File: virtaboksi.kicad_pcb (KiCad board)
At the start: 2 copper layers, 50 x 71.9 mm, 61 parts, among them J1 Panel_01x08, J2 Ext_01x05, J3 Powerpole 01x02, J4 Powerpole 01x02, J5 Powerpole 01x02, J6 Conn_01x03_Male, J7 TagConnect_TC2030-NL, Q1 2N7002, Q2 IRF4905, Q3 IRF4905, Q4 2N7002, Q5 IRF4905, Q6 IRF4905, Q7 2N7002, Q8 IRF4905, Q9 IRF4905, U1 SRV05-4, U2 AMSRI-783.3-NZ, U3 STM8S003F3P, U4 SRV05-4, U5 SP3485EN

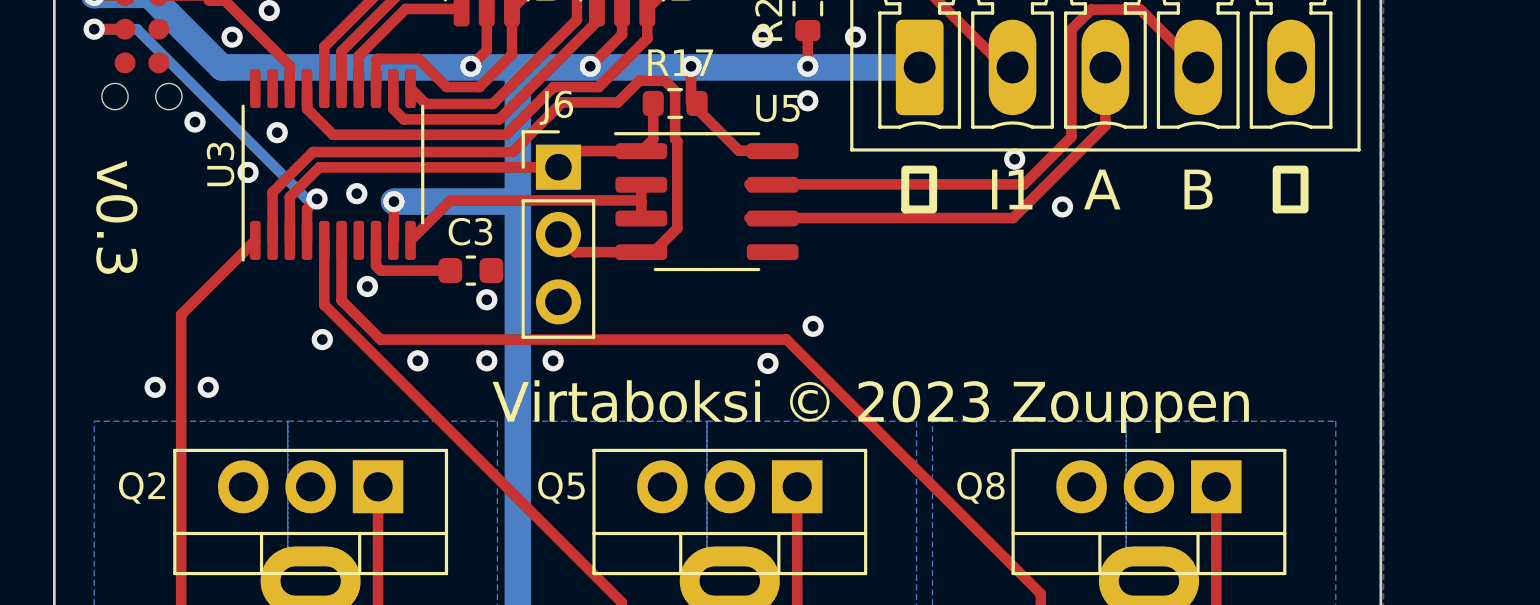
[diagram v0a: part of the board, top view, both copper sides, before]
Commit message: Update silkscreen, change revision to 0.4
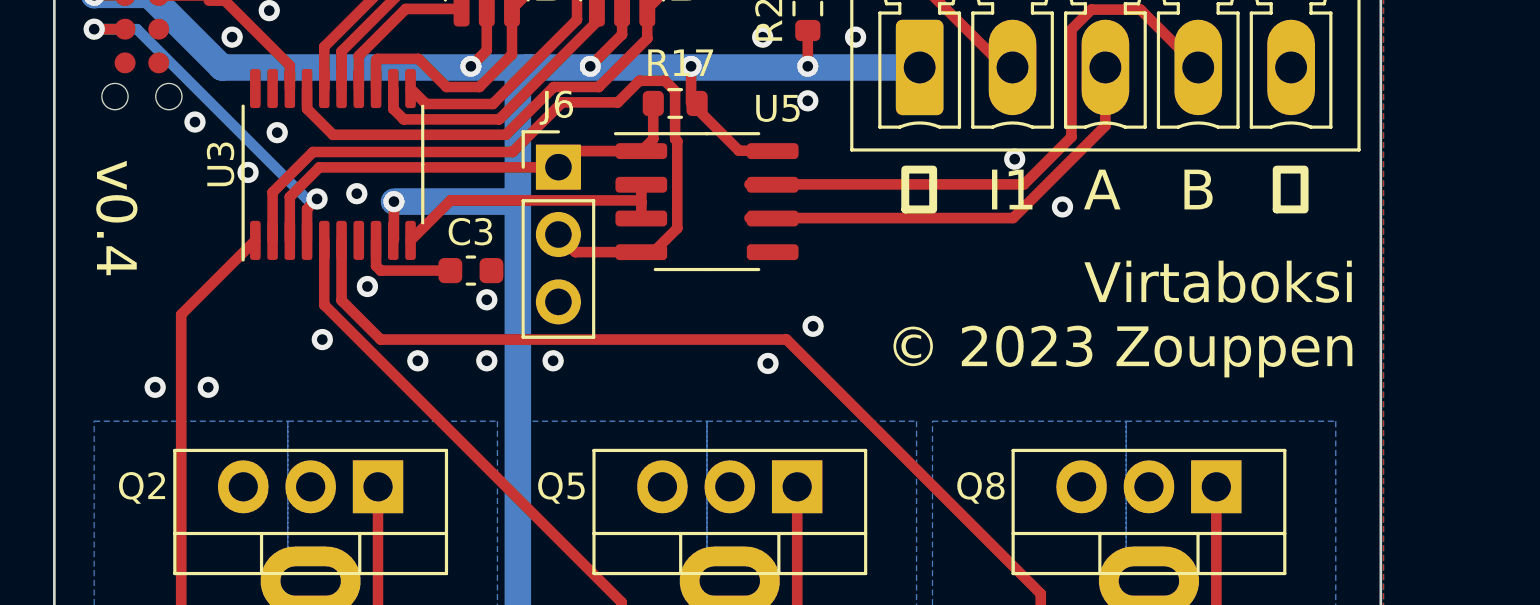
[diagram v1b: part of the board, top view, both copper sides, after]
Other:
- board text added: "${TITLE} © ${COMMENT1} ${COMPANY}"
- board text added: "I2"
- board text added: "I3"
- board text added: "I4"
- board text added: "L1"
- board text added: "L2"
- board text added: "L3"
- board text added: "RX"
- board text added: "TX"
- board text removed: "Virtaboksi © 2023 Zouppen"
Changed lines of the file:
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@@
   (paper "A4")
   (title_block
-    (rev "0.3")
+    (title "Virtaboksi")
+    (date "2023-09-26")
+    (rev "0.4")
+    (company "Zouppen")
+    (comment 1 "2023")
   )
   (layers
@@
     ) (layer "B.Mask") (width 0) (fill solid))
   (gr_rect (start 107.5 40) (end 157.5 111.9) (layer "Edge.Cuts") (width 0.1) (fill none))
+  (gr_text "⏚" (at 128.3 64.7) (layer "B.SilkS")
+    (effects (font (size 1.5 1.5) (thickness 0.3)) (justify right mirror))
+  )
+  (gr_text "I4" (at 125.6 48.6) (layer "B.SilkS")
+    (effects (font (size 1.5 1.5) (thickness 0.3)) (justify mirror))
+  )
+  (gr_text "I3" (at 122.2 48.6) (layer "B.SilkS")
+    (effects (font (size 1.5 1.5) (thickness 0.3)) (justify mirror))
+  )
+  (gr_text "L3" (at 139.7 48.7) (layer "B.SilkS")
+    (effects (font (size 1.5 1.5) (thickness 0.3)) (justify mirror))
+  )
+  (gr_text "⏚" (at 129.2 48.6) (layer "B.SilkS")
+    (effects (font (size 1.5 1.5) (thickness 0.3)) (justify mirror))
+  )
+  (gr_text "TX" (at 128.2 61.9) (layer "B.SilkS")
+    (effects (font (size 1.5 1.5) (thickness 0.3)) (justify right mirror))
+  )
+  (gr_text "⏚" (at 143.2 48.6) (layer "B.SilkS")
+    (effects (font (size 1.5 1.5) (thickness 0.3)) (justify mirror))
+  )
+  (gr_text "RX" (at 128.3 59.5) (layer "B.SilkS")
+    (effects (font (size 1.5 1.5) (thickness 0.3)) (justify right mirror))
+  )
+  (gr_text "L2" (at 136.1 48.6) (layer "B.SilkS")
+    (effects (font (size 1.5 1.5) (thickness 0.3)) (justify mirror))
+  )
+  (gr_text "L1" (at 132.6 48.6) (layer "B.SilkS")
+    (effects (font (size 1.5 1.5) (thickness 0.3)) (justify mirror))
+  )
+  (gr_text "I2" (at 118.7 48.6) (layer "B.SilkS")
+    (effects (font (size 1.5 1.5) (thickness 0.3)) (justify mirror))
+  )
   (gr_text "⏚" (at 154.1 60.3) (layer "F.SilkS")
     (effects (font (size 1.5 1.5) (thickness 0.3)))
@@
     (effects (font (size 1.5 1.5) (thickness 0.3)))
   )
-  (gr_text "Virtaboksi © 2023 Zouppen" (at 124 68.3) (layer "F.SilkS")
-    (effects (font (size 1.5 1.5) (thickness 0.3)) (justify left))
+  (gr_text "${TITLE}\n© ${COMMENT1} ${COMPANY}" (at 156.6 65) (layer "F.SilkS")
+    (effects (font (size 1.5 1.5) (thickness 0.3)) (justify right))
   )
   (gr_text "I1" (at 143.6 60.3) (layer "F.SilkS")

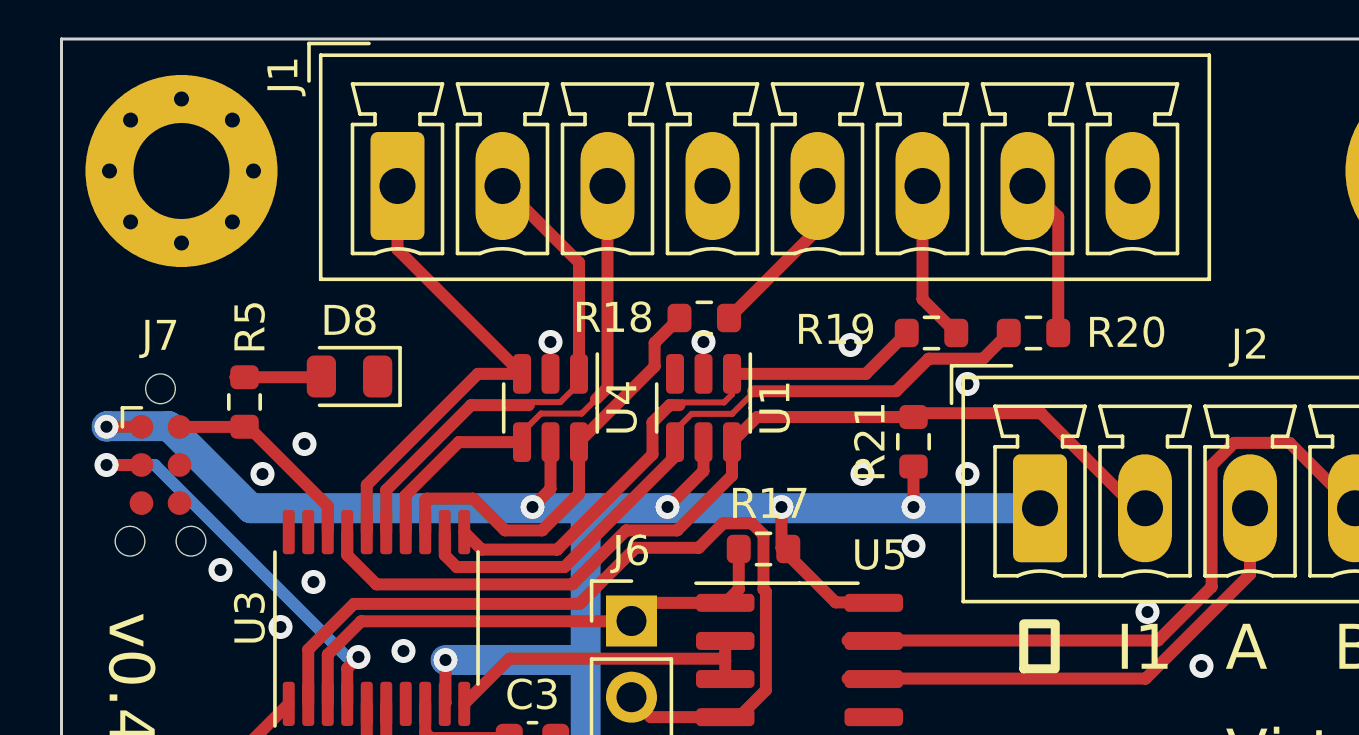
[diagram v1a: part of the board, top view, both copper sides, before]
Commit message: Minor cosmetic PCB changes
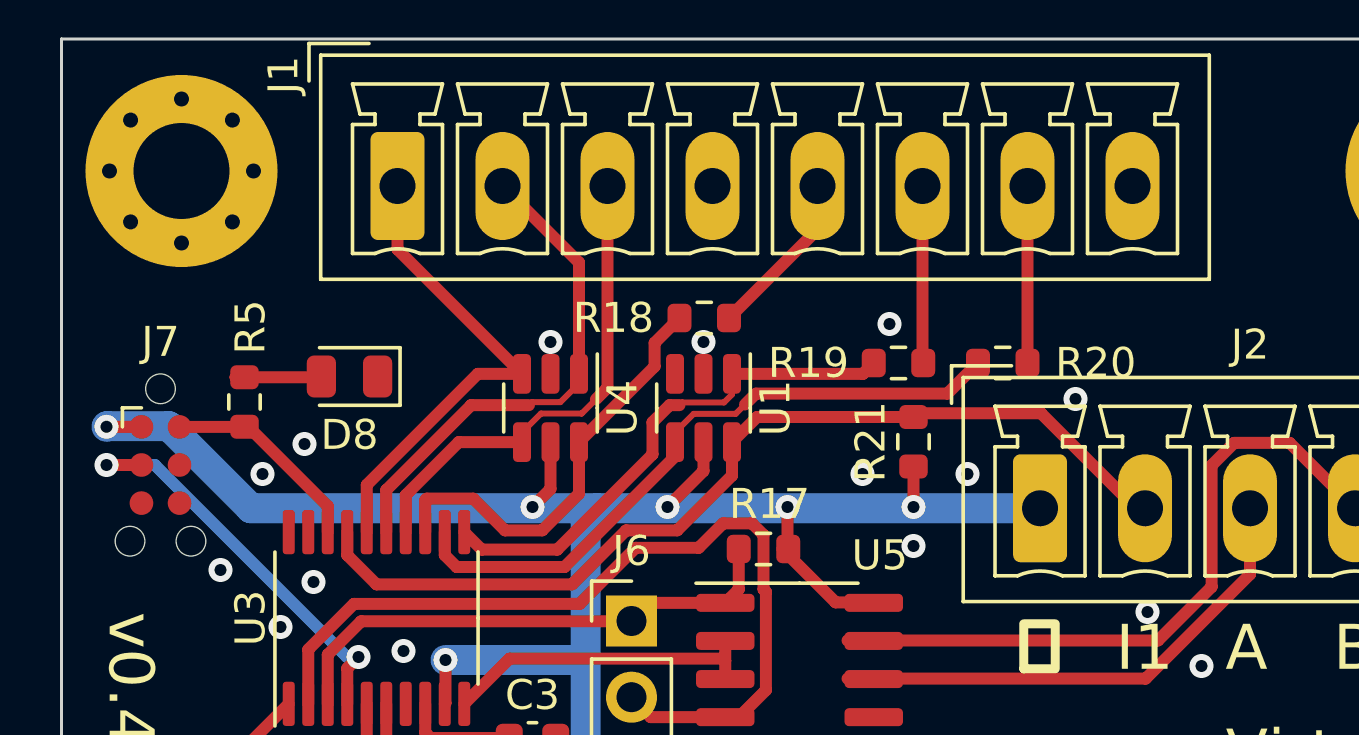
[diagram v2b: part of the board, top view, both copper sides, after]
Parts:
- moved R19 1.49 mm to (135.4, 50.8)
- moved R20 1.43 mm to (138.9, 50.8)
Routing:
- net /LED2: track 19.0 -> 17.5 mm
- net /LED3: track 23.5 -> 22.4 mm
- net Net-(J1-Pad7): track 5.32 -> 5.90 mm
- net Net-(J1-Pad6): track 5.37 -> 5.91 mm
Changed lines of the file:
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@@
     (property "Sheetname" "")
     (attr exclude_from_pos_files)
-    (fp_text reference "J7" (at -4.3 0 180) (layer "F.SilkS")
+    (fp_text reference "J7" (at -4.1 0 180) (layer "F.SilkS")
       (effects (font (size 1 1) (thickness 0.15)))
     )
@@
     (property "Sheetname" "")
     (attr smd)
-    (fp_text reference "D8" (at 0 1.85) (layer "F.SilkS")
+    (fp_text reference "D8" (at 0 -1.95) (layer "F.SilkS")
       (effects (font (size 1 1) (thickness 0.15)))
     )
@@
   )
   (footprint "Resistor_SMD:R_0603_1608Metric" (layer "F.Cu")
-    (at 139.9 49.8 180)
+    (at 138.875 50.8 180)
     (descr "Resistor SMD 0603 (1608 Metric), square (rectangular) end terminal, IPC_7351 nominal, (Body size source: IPC-SM-782 page 72, https://www.pcb-3d.com/wordpress/wp-content/uploads/ipc-sm-782a_amendment_1_and_2.pdf), generated with kicad-footprint-generator")
     (tags "resistor")
@@
   )
   (footprint "Resistor_SMD:R_0603_1608Metric" (layer "F.Cu")
-    (at 136.5 49.8 180)
+    (at 135.4 50.8 180)
     (descr "Resistor SMD 0603 (1608 Metric), square (rectangular) end terminal, IPC_7351 nominal, (Body size source: IPC-SM-782 page 72, https://www.pcb-3d.com/wordpress/wp-content/uploads/ipc-sm-782a_amendment_1_and_2.pdf), generated with kicad-footprint-generator")
     (tags "resistor")
@@
     (property "Sheetname" "")
     (attr smd)
-    (fp_text reference "R19" (at 3.2 0.1) (layer "F.SilkS")
+    (fp_text reference "R19" (at 3 0) (layer "F.SilkS")
       (effects (font (size 1 1) (thickness 0.15)))
     )
@@
   (via (at 126.3 66.7) (size 0.8) (drill 0.4) (layers "F.Cu" "B.Cu") (free) (net 1))
   (via (at 112.8 57.7) (size 0.8) (drill 0.4) (layers "F.Cu" "B.Cu") (free) (net 1))
-  (via (at 133.8 50.2) (size 0.8) (drill 0.4) (layers "F.Cu" "B.Cu") (free) (net 1))
+  (via (at 135.1 49.5) (size 0.8) (drill 0.4) (layers "F.Cu" "B.Cu") (free) (net 1))
   (via (at 114.2 54.5) (size 0.8) (drill 0.4) (layers "F.Cu" "B.Cu") (free) (net 1))
   (via (at 119.3 63.9) (size 0.8) (drill 0.4) (layers "F.Cu" "B.Cu") (free) (net 1))
@@
   (via (at 113.3 67.7) (size 0.8) (drill 0.4) (layers "F.Cu" "B.Cu") (free) (net 1))
   (via (at 134.4 66.8) (size 0.8) (drill 0.4) (layers "F.Cu" "B.Cu") (free) (net 1))
-  (via (at 137.7 51.5) (size 0.8) (drill 0.4) (layers "F.Cu" "B.Cu") (free) (net 1))
+  (via (at 141.3 52) (size 0.8) (drill 0.4) (layers "F.Cu" "B.Cu") (free) (net 1))
   (via (at 114.8 59.6) (size 0.8) (drill 0.4) (layers "F.Cu" "B.Cu") (free) (net 1))
   (via (at 115.9 58.1) (size 0.8) (drill 0.4) (layers "F.Cu" "B.Cu") (free) (net 1))
@@
   (segment (start 123.8 55) (end 123.2 55.6) (width 0.4) (layer "F.Cu") (net 6))
   (segment (start 133.7 58.78) (end 133.305 58.78) (width 0.4) (layer "F.Cu") (net 6))
-  (segment (start 131.5 55.6) (end 131.5 56.975) (width 0.4) (layer "F.Cu") (net 6))
   (segment (start 110.16 52.925) (end 110.165 52.93) (width 0.4) (layer "F.Cu") (net 6))
+  (segment (start 131.7 55.6) (end 131.7 56.975) (width 0.4) (layer "F.Cu") (net 6))
   (segment (start 135.9 54.25) (end 135.9 55.6) (width 0.4) (layer "F.Cu") (net 6))
   (segment (start 120.3 60.7) (end 120.3 62.1375) (width 0.4) (layer "F.Cu") (net 6))
-  (segment (start 131.5 56.975) (end 131.525 57) (width 0.4) (layer "F.Cu") (net 6))
   (segment (start 127.7 55.6) (end 128.9 54.4) (width 0.4) (layer "F.Cu") (net 6))
+  (segment (start 131.7 56.975) (end 131.725 57) (width 0.4) (layer "F.Cu") (net 6))
   (segment (start 119.975 104.1) (end 121.4 104.1) (width 0.4) (layer "F.Cu") (net 6))
   (segment (start 120.3 62.1375) (end 120.275 62.1625) (width 0.4) (layer "F.Cu") (net 6))
@@
   (via (at 127.7 55.6) (size 0.8) (drill 0.4) (layers "F.Cu" "B.Cu") (net 6))
   (via (at 123.2 55.6) (size 0.8) (drill 0.4) (layers "F.Cu" "B.Cu") (net 6))
-  (via (at 131.5 55.6) (size 0.8) (drill 0.4) (layers "F.Cu" "B.Cu") (net 6))
+  (via (at 131.7 55.6) (size 0.8) (drill 0.4) (layers "F.Cu" "B.Cu") (net 6))
   (via (at 109 52.925) (size 0.8) (drill 0.4) (layers "F.Cu" "B.Cu") (net 6))
   (via (at 121.4 104.1) (size 0.8) (drill 0.4) (layers "F.Cu" "B.Cu") (net 6))
@@
   (segment (start 129.75 49.3) (end 132.7 46.35) (width 0.4) (layer "F.Cu") (net 14))
   (segment (start 132.7 46.35) (end 132.7 44.9) (width 0.4) (layer "F.Cu") (net 14))
-  (segment (start 136.2 48.675) (end 136.2 44.9) (width 0.4) (layer "F.Cu") (net 15))
-  (segment (start 137.325 49.8) (end 136.2 48.675) (width 0.4) (layer "F.Cu") (net 15))
-  (segment (start 140.725 49.8) (end 140.725 45.925) (width 0.4) (layer "F.Cu") (net 16))
-  (segment (start 140.725 45.925) (end 139.7 44.9) (width 0.4) (layer "F.Cu") (net 16))
+  (segment (start 136.2 50.775) (end 136.225 50.8) (width 0.4) (layer "F.Cu") (net 15))
+  (segment (start 136.2 44.9) (end 136.2 50.775) (width 0.4) (layer "F.Cu") (net 15))
+  (segment (start 139.7 44.9) (end 139.7 50.8) (width 0.4) (layer "F.Cu") (net 16))
   (segment (start 129.85 54.553087) (end 129.85 53.4375) (width 0.4) (layer "F.Cu") (net 17))
   (segment (start 118.001177 58.18) (end 124.52 58.18) (width 0.4) (layer "F.Cu") (net 17))
@@
   (segment (start 119.625 55.375) (end 119.625 56.4375) (width 0.4) (layer "F.Cu") (net 27))
   (segment (start 121.223822 55.32) (end 119.68 55.32) (width 0.4) (layer "F.Cu") (net 27))
-  (segment (start 134.3125 51.1625) (end 129.85 51.1625) (width 0.4) (layer "F.Cu") (net 28))
   (segment (start 128.19 52.115) (end 128.1 52.205) (width 0.2) (layer "F.Cu") (net 28))
-  (segment (start 135.675 49.8) (end 134.3125 51.1625) (width 0.4) (layer "F.Cu") (net 28))
   (segment (start 127.770467 52.205) (end 127.2 52.775467) (width 0.4) (layer "F.Cu") (net 28))
   (segment (start 129.85 51.1625) (end 129.85 51.85) (width 0.2) (layer "F.Cu") (net 28))
   (segment (start 124.025587 57.02) (end 121.5075 57.02) (width 0.4) (layer "F.Cu") (net 28))
   (segment (start 129.85 51.85) (end 129.585 52.115) (width 0.2) (layer "F.Cu") (net 28))
+  (segment (start 134.2125 51.1625) (end 134.575 50.8) (width 0.4) (layer "F.Cu") (net 28))
   (segment (start 127.2 52.775467) (end 127.2 53.845587) (width 0.4) (layer "F.Cu") (net 28))
+  (segment (start 129.85 51.1625) (end 134.2125 51.1625) (width 0.4) (layer "F.Cu") (net 28))
   (segment (start 127.2 53.845587) (end 124.025587 57.02) (width 0.4) (layer "F.Cu") (net 28))
   (segment (start 121.5075 57.02) (end 120.925 56.4375) (width 0.4) (layer "F.Cu") (net 28))
   (segment (start 129.585 52.115) (end 128.19 52.115) (width 0.2) (layer "F.Cu") (net 28))
   (segment (start 128.1 52.205) (end 127.770467 52.205) (width 0.4) (layer "F.Cu") (net 28))
-  (segment (start 130.55 51.8) (end 129.855 52.495) (width 0.2) (layer "F.Cu") (net 29))
-  (segment (start 138.22 50.655) (end 136.405 50.655) (width 0.4) (layer "F.Cu") (net 29))
+  (segment (start 127.95 53.116888) (end 128.571888 52.495) (width 0.2) (layer "F.Cu") (net 29))
   (segment (start 127.95 53.915831) (end 127.95 53.4375) (width 0.4) (layer "F.Cu") (net 29))
-  (segment (start 139.075 49.8) (end 138.22 50.655) (width 0.4) (layer "F.Cu") (net 29))
-  (segment (start 129.855 52.495) (end 128.505 52.495) (width 0.2) (layer "F.Cu") (net 29))
-  (segment (start 130.55 51.7425) (end 130.55 51.8) (width 0.2) (layer "F.Cu") (net 29))
+  (segment (start 129.972256 52.495) (end 130.283628 52.183628) (width 0.2) (layer "F.Cu") (net 29))
+  (segment (start 130.647256 51.82) (end 130.283628 52.183628) (width 0.4) (layer "F.Cu") (net 29))
+  (segment (start 127.95 53.4375) (end 127.95 53.116888) (width 0.2) (layer "F.Cu") (net 29))
+  (segment (start 137.03 51.82) (end 130.647256 51.82) (width 0.4) (layer "F.Cu") (net 29))
+  (segment (start 138.05 50.8) (end 137.03 51.82) (width 0.4) (layer "F.Cu") (net 29))
   (segment (start 127.95 53.4375) (end 127.95 53.05) (width 0.2) (layer "F.Cu") (net 29))
   (segment (start 124.265831 57.6) (end 127.95 53.915831) (width 0.4) (layer "F.Cu") (net 29))
-  (segment (start 127.95 53.05) (end 128.505 52.495) (width 0.2) (layer "F.Cu") (net 29))
+  (segment (start 128.571888 52.495) (end 129.972256 52.495) (width 0.2) (layer "F.Cu") (net 29))
   (segment (start 120.275 57.203823) (end 120.671177 57.6) (width 0.4) (layer "F.Cu") (net 29))
   (segment (start 120.671177 57.6) (end 124.265831 57.6) (width 0.4) (layer "F.Cu") (net 29))
-  (segment (start 135.3175 51.7425) (end 130.55 51.7425) (width 0.4) (layer "F.Cu") (net 29))
-  (segment (start 136.405 50.655) (end 135.3175 51.7425) (width 0.4) (layer "F.Cu") (net 29))
   (segment (start 120.275 56.4375) (end 120.275 57.203823) (width 0.4) (layer "F.Cu") (net 29))
   (segment (start 124.77 58.83) (end 126.64 56.96) (width 0.4) (layer "F.Cu") (net 30))
